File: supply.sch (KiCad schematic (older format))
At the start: 0 parts

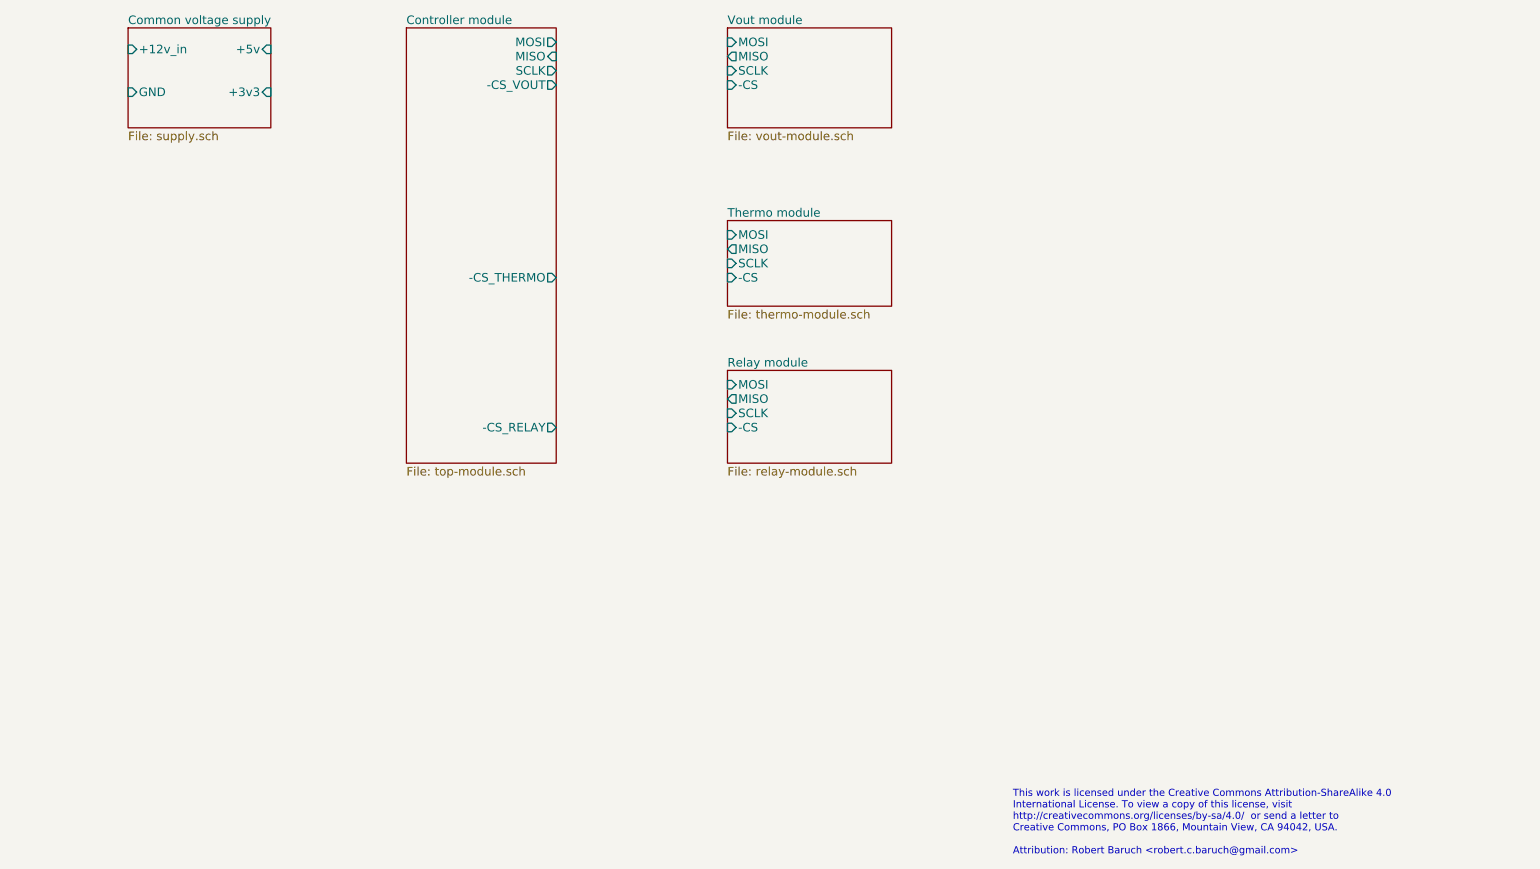
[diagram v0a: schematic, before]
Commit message: thermo module block diagram, more skeletal signals
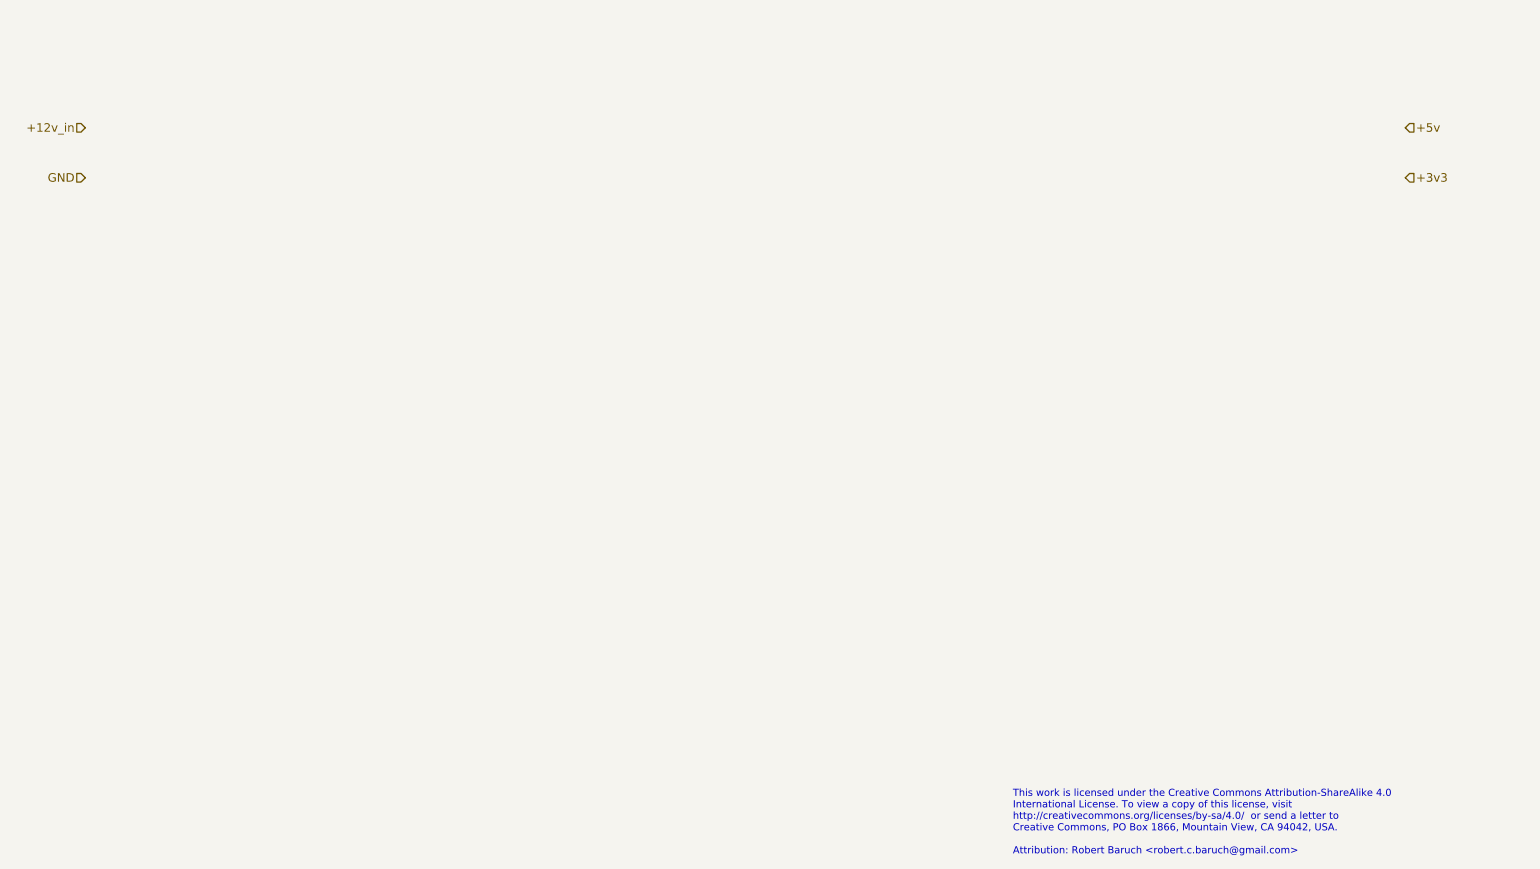
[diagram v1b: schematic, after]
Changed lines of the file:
@@
 $Descr A4 11693 8268
 encoding utf-8
-Sheet 1 6
+Sheet 2 6
 Title ""
 Date ""
@@
 Comment4 ""
 $EndDescr
+Text HLabel 1250 1950 0    60   Input ~ 0
++12v_in
+Text HLabel 1250 2300 0    60   Input ~ 0
+GND
+Text HLabel 10500 1950 2    60   Input ~ 0
++5v
+Text HLabel 10500 2300 2    60   Input ~ 0
++3v3
 $Bitmap
 Pos 7350 6700
@@
 Text Notes 7750 7050 0    50   ~ 0
 This work is licensed under the Creative Commons Attribution-ShareAlike 4.0 \nInternational License. To view a copy of this license, visit \nhttp://creativecommons.org/licenses/by-sa/4.0/  or send a letter to \nCreative Commons, PO Box 1866, Mountain View, CA 94042, USA.\n\nAttribution: Robert Baruch <robert.c.baruch@gmail.com>
-$Sheet
-S 1550 1250 1000 700
-U 57F7AE9A
-F0 "Common voltage supply" 60
-F1 "supply.sch" 60
-F2 "+12v_in" I L 1550 1400 60
-F3 "GND" I L 1550 1700 60
-F4 "+5v" I R 2550 1400 60
-F5 "+3v3" I R 2550 1700 60
-$EndSheet
-$Sheet
-S 3500 1250 1050 3050
-U 57F7AE9D
-F0 "Controller module" 60
-F1 "top-module.sch" 60
-F2 "MOSI" O R 4550 1350 60
-F3 "MISO" I R 4550 1450 60
-F4 "SCLK" O R 4550 1550 60
-F5 "-CS_THERMO" O R 4550 3000 60
-F6 "-CS_VOUT" O R 4550 1650 60
-F7 "-CS_RELAY" O R 4550 4050 60
-$EndSheet
-$Sheet
-S 5750 1250 1150 700
-U 57F7AEA0
-F0 "Vout module" 60
-F1 "vout-module.sch" 60
-F2 "MOSI" I L 5750 1350 60
-F3 "MISO" O L 5750 1450 60
-F4 "SCLK" I L 5750 1550 60
-F5 "-CS" I L 5750 1650 60
-$EndSheet
-$Sheet
-S 5750 2600 1150 600
-U 57F7AEA3
-F0 "Thermo module" 60
-F1 "thermo-module.sch" 60
-F2 "MOSI" I L 5750 2700 60
-F3 "MISO" O L 5750 2800 60
-F4 "SCLK" I L 5750 2900 60
-F5 "-CS" I L 5750 3000 60
-$EndSheet
-$Sheet
-S 5750 3650 1150 650
-U 57F7AEA8
-F0 "Relay module" 60
-F1 "relay-module.sch" 60
-F2 "MOSI" I L 5750 3750 60
-F3 "MISO" O L 5750 3850 60
-F4 "SCLK" I L 5750 3950 60
-F5 "-CS" I L 5750 4050 60
-$EndSheet
 $EndSCHEMATC
